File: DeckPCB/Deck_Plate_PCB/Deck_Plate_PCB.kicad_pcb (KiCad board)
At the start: 2 copper layers, 124.1 x 104 mm, 76 parts, among them J1 Raspberry_Pi_2_3, J2 NASA_Telemetry_Interface, J3 NASA PWR_Interface, J8 Board_to_Board, J9 Power, P1 Digital, P10 CONN_01X01, P11 CONN_01X01, P12 CONN_01X01, P13 CONN_01X01, P2 Power, P3 Analog, P4 Analog, P5 PWM, P6 PWM, P7 Communication, P8 CONN_01X01, P9 CONN_01X01, Q2 2N7000, Q3 2N7000, U1 LF356, U10 MAX1044, U11 LF356, U12 LF356, U2 LM2576T-5, U3 D24V25F9, U4 LF356, U5 LM2576T-5, U6 SF_Logic_Level_Conv, U7 Lidar_RangeFinder, U8 ADXL377, U9 TTL_Camera

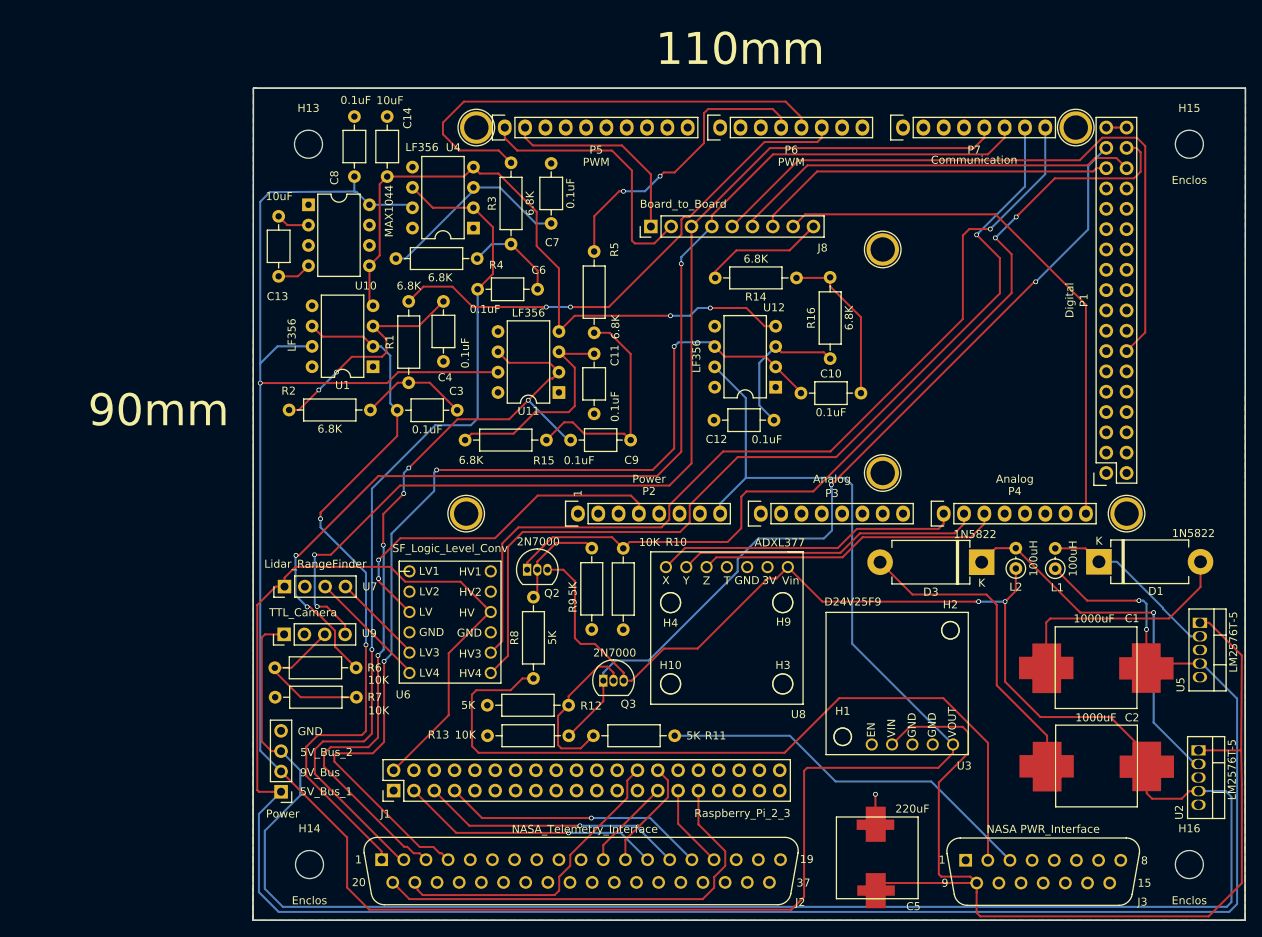
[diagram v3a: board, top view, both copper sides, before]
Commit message: Updated main board to incorporate all 16-bits of telemetry lines
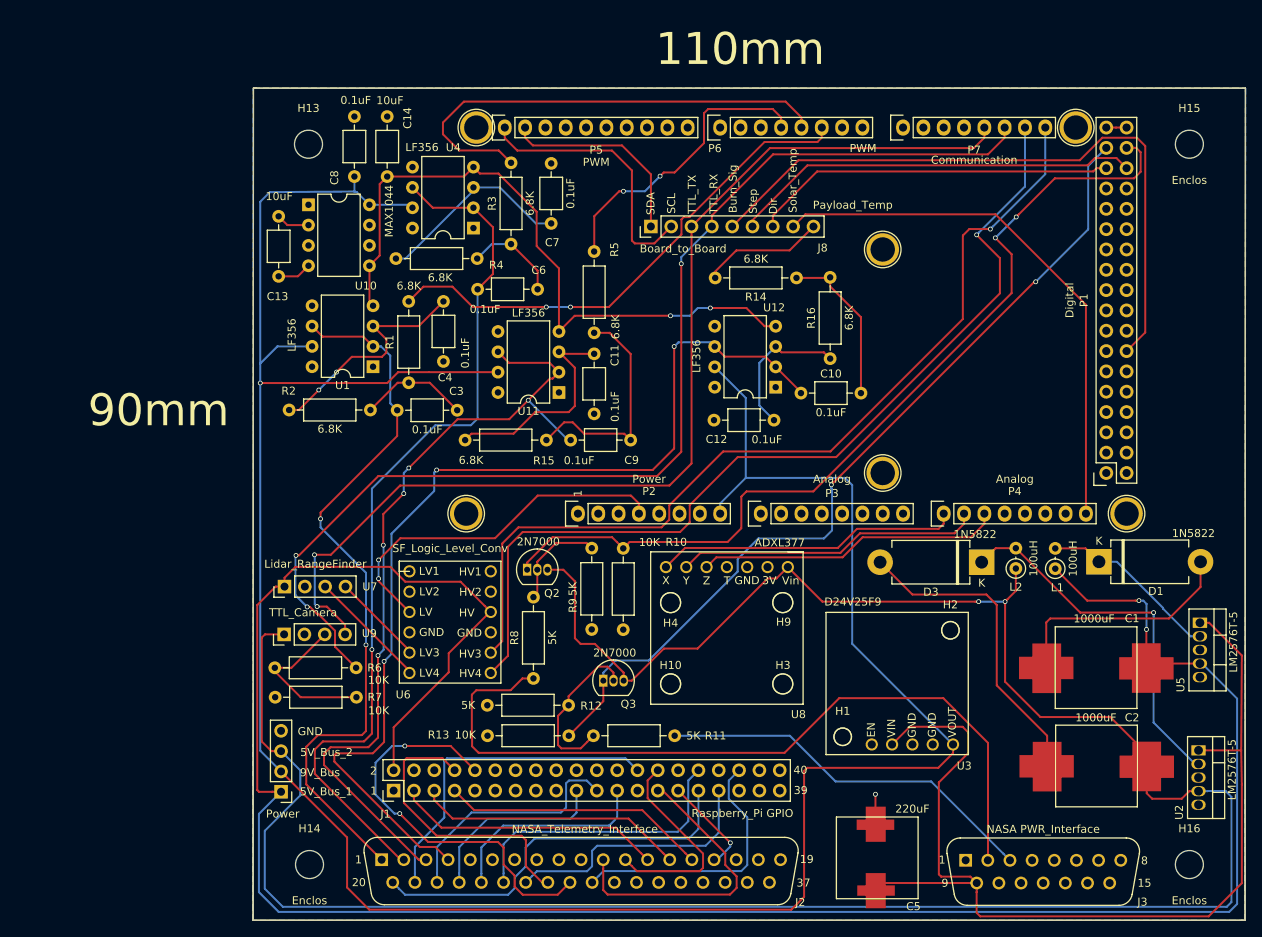
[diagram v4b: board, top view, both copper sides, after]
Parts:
- J1: value Raspberry_Pi_2_3 -> Raspberry_Pi GPIO
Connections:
- net Net-(J1-Pad11) renamed /Bit_16
- J1 pad 10: Net-(J1-Pad10) -> /Bit_14
- J1 pad 19: Net-(J1-Pad19) -> /Bit_9
- J1 pad 21: Net-(J1-Pad21) -> /Bit_8
- J1 pad 23: Net-(J1-Pad23) -> /Bit_10
- J1 pad 32: Net-(J1-Pad32) -> /Bit_11
- J1 pad 33: Net-(J1-Pad33) -> /Bit_12
- J1 pad 36: Net-(J1-Pad36) -> /Bit_15
- J1 pad 8: Net-(J1-Pad8) -> /Bit_13
- J2 pad 22: Net-(J2-Pad22) -> /Bit_8
- J2 pad 23: Net-(J2-Pad23) -> /Bit_9
- J2 pad 24: Net-(J2-Pad24) -> /Bit_10
- J2 pad 25: Net-(J2-Pad25) -> /Bit_11
- J2 pad 26: Net-(J2-Pad26) -> /Bit_12
- J2 pad 27: Net-(J2-Pad27) -> /Bit_13
- J2 pad 28: Net-(J2-Pad28) -> /Bit_14
- J2 pad 29: Net-(J2-Pad29) -> /Bit_15
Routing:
- net /Bit_14: track 0.00 -> 50.7 mm, vias 0 -> 2
- net /Bit_13: track 0.00 -> 36.4 mm
- net /Bit_11: track 0.00 -> 36.0 mm
- net /Bit_15: track 0.00 -> 33.6 mm
- net /Bit_12: track 0.00 -> 33.1 mm
- net /Bit_8: track 0.00 -> 30.1 mm
- net /Bit_10: track 0.00 -> 26.3 mm
- net /Bit_0: track 11.5 -> 37.7 mm
- net /Bit_9: track 0.00 -> 23.6 mm
- net /Bit_1: track 13.9 -> 26.1 mm
- net /Bit_6: track 55.7 -> 49.2 mm
- net /Bit_7: track 37.9 -> 41.6 mm
- net /Bit_5: track 10.5 -> 12.4 mm, vias 0 -> 1
- net /Bit_3: track 33.0 -> 33.7 mm, vias 1 -> 0
- net /Bit_2: track 32.8 -> 33.5 mm, vias 1 -> 0
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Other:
- board text added: "2"
- board text added: "39"
- board text added: "40"
- board text added: "Burn_Sig"
- board text added: "Dir"
- board text added: "Payload_Temp"
- board text added: "SCL"
- board text added: "SDA"
- board text added: "Solar_Temp"
- board text added: "Step"
- board text added: "TTL_RX"
- board text added: "TTL_TX"

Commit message: Updated PCB for NASA analog lines and signal conditioning circuitry. Added Gerber file ZIP for DECK_PLATE_MAIN
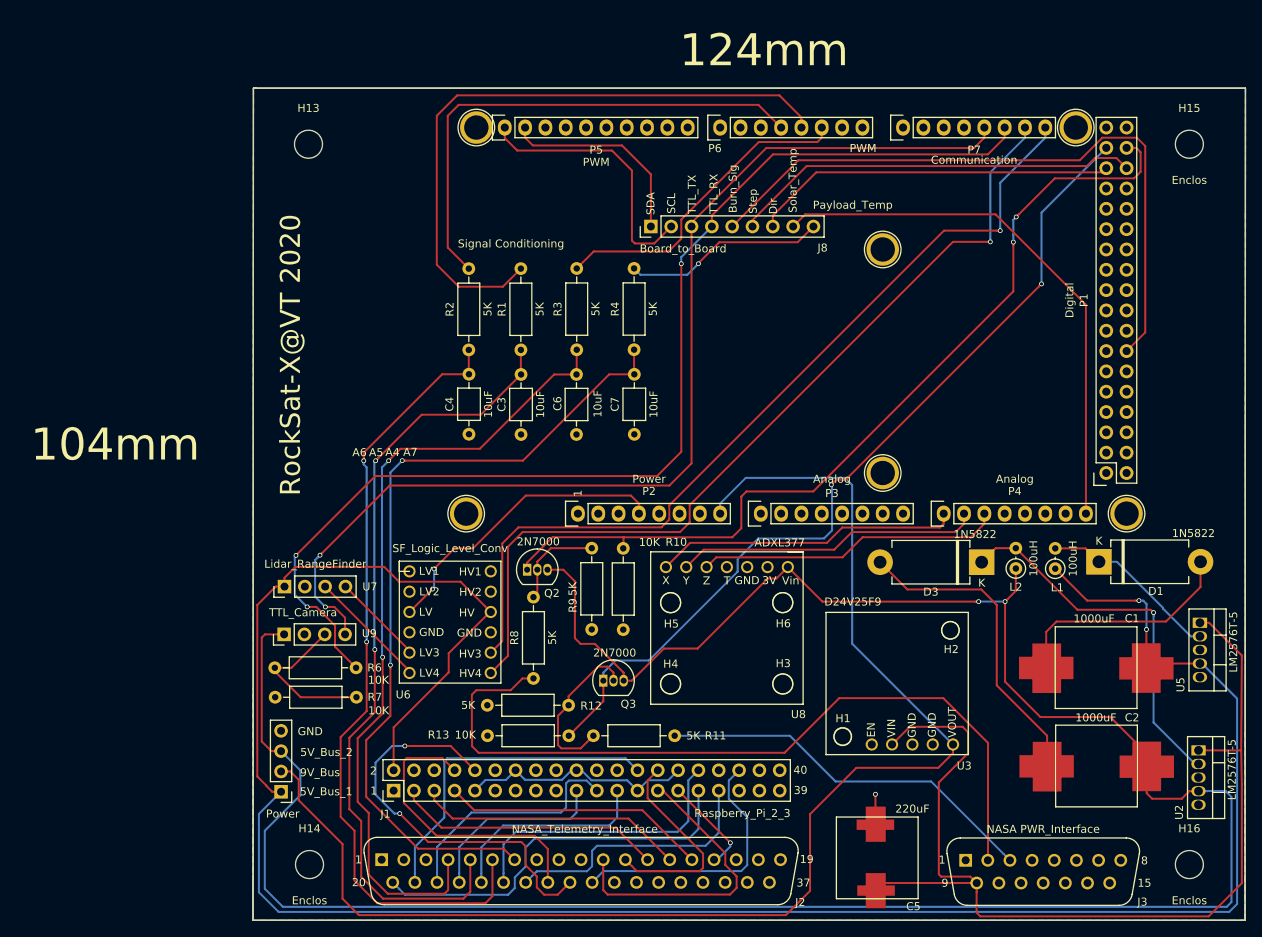
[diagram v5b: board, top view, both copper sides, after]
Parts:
- removed C10, C11, C12, C8, C9: 0.1uF, Capacitor_THT:C_Axial_L3.8mm_D2.6mm_P7.50mm_Horizontal
- removed C13, C14: 10uF, Capacitor_THT:C_Axial_L3.8mm_D2.6mm_P7.50mm_Horizontal
- removed H10, H9: Accel_mount, MountingHole:MountingHole_2.5mm
- removed R14, R15, R16, R5: 6.8K, Resistor_THT:R_Axial_DIN0207_L6.3mm_D2.5mm_P10.16mm_Horizontal
- removed U1, U11, U12, U4: LF356, Package_DIP:DIP-8_W7.62mm
- removed U10: MAX1044, Package_DIP:DIP-8_W7.62mm
- added H5: Accel_mount, Deck_Plate_PCB:Accel_MountingHole_2.5mm, F.Cu at (131.1, 108.3)
- added H6: Accel_mount, Deck_Plate_PCB:Accel_MountingHole_2.5mm, F.Cu at (145.1, 108.3)
- C3, C4, C6, C7: value 0.1uF -> 10uF
- H1, H2: footprint MountingHole:MountingHole_2.2mm_M2 -> Deck_Plate_PCB:9V_MountingHole_2.2mm
- H3, H4: footprint MountingHole:MountingHole_2.5mm -> Deck_Plate_PCB:Accel_MountingHole_2.5mm
- J1: value Raspberry_Pi GPIO -> Raspberry_Pi_2_3
- R1, R2, R3, R4: value 6.8K -> 5K
- moved R4 31.9 mm to (126.5, 76.7), turned to 90 degrees
- moved C7 28.3 mm to (126.6, 87.2)
- moved R2 23.7 mm to (105.9, 76.7), turned to 90 degrees
- moved C6 22.0 mm to (119.3, 87.3), turned to 90 degrees
- moved C4 16.9 mm to (105.9, 87.2), turned to 90 degrees
- moved C3 15.8 mm to (112.4, 87.3), turned to 90 degrees
- moved R3 15.6 mm to (119.4, 76.7)
- moved R1 14.6 mm to (112.4, 76.7)
- moved H4 10.2 mm to (131.1, 118.4)
- moved H3 5.96 mm to (141.1, 114.0)
- moved H2 0.06 mm to (166.1, 111.8)
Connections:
- C3 pad 1: /NASA_Analog_1_OUT -> GND
- C3 pad 2: Net-(C3-Pad2) -> /NASA_Analog_5_OUT
- C4 pad 1: Net-(C4-Pad1) -> GND
- C4 pad 2: GND -> /NASA_Analog_6_OUT
- C6 pad 1: /NASA_Analog_2_OUT -> GND
- C6 pad 2: Net-(C6-Pad2) -> /NASA_Analog_4_OUT
- C7 pad 1: Net-(C7-Pad1) -> GND
- C7 pad 2: GND -> /NASA_Analog_7_OUT
- J2 pad 1: /NASA_Analog_1_OUT -> Net-(J2-Pad1)
- J2 pad 2: /NASA_Analog_2_OUT -> Net-(J2-Pad2)
- J2 pad 3: /NASA_Analog_3_OUT -> Net-(J2-Pad3)
- J2 pad 5: Net-(J2-Pad5) -> /NASA_Analog_5_OUT
- J2 pad 6: Net-(J2-Pad6) -> /NASA_Analog_6_OUT
- J2 pad 7: Net-(J2-Pad7) -> /NASA_Analog_7_OUT
- P1 pad 36: Net-(P1-Pad35) -> Net-(P1-Pad36)
- P6 pad 4: /NASA_Analog_3_IN -> /NASA_Analog_6_IN
- P6 pad 5: /NASA_Analog_2_IN -> /NASA_Analog_5_IN
- P6 pad 6: /NASA_Analog_1_IN -> /NASA_Analog_4_IN
- R1 pad 1: Net-(C3-Pad2) -> /NASA_Analog_5_OUT
- R1 pad 2: /NASA_Analog_1_IN -> /NASA_Analog_5_IN
- R2 pad 1: Net-(C4-Pad1) -> /NASA_Analog_6_OUT
- R2 pad 2: Net-(C3-Pad2) -> /NASA_Analog_6_IN
- R3 pad 1: Net-(C6-Pad2) -> /NASA_Analog_4_OUT
- R3 pad 2: /NASA_Analog_2_IN -> /NASA_Analog_4_IN
- R4 pad 1: Net-(C7-Pad1) -> /NASA_Analog_7_OUT
- R4 pad 2: Net-(C6-Pad2) -> /PayloadTemp
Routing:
- net /9V_Bus: track 318.0 -> 169.2 mm, vias 1 -> 0
- net /NASA_Analog_2_OUT: track 110.9 -> 0.00 mm, vias 1 -> 0
- net /NASA_Analog_7_OUT: track 0.00 -> 102.3 mm, vias 0 -> 2
- net /NASA_Analog_3_OUT: track 101.7 -> 0.00 mm, vias 5 -> 0
- net /NASA_Analog_6_OUT: track 0.00 -> 99.3 mm, vias 0 -> 2
- net /NASA_Analog_5_OUT: track 0.00 -> 98.9 mm, vias 0 -> 2
- net /NASA_Analog_1_OUT: track 91.2 -> 0.00 mm, vias 2 -> 0
- net /-9V_Bus: track 84.1 -> 0.00 mm, vias 2 -> 0
- net /NASA_Analog_5_IN: track 0.00 -> 80.3 mm
- net /NASA_Analog_1_IN: track 64.6 -> 0.00 mm, vias 2 -> 0
- net /NASA_Analog_6_IN: track 0.00 -> 63.6 mm
- net /NASA_Analog_2_IN: track 59.4 -> 0.00 mm
- net /NASA_Analog_4_IN: track 0.00 -> 40.1 mm
- net /NASA_Analog_3_IN: track 37.2 -> 0.00 mm, vias 2 -> 0
- net GND: track 3.89 -> 33.4 mm
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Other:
- board text added: "104mm"
- board text added: "124mm"
- board text added: "A4"
- board text added: "A5"
- board text added: "A6"
- board text added: "A7"
- board text added: "RockSat-X@VT 2020"
- board text added: "Signal Conditioning"
- board text removed: "110mm"
- board text removed: "90mm"

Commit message: Updated Main_Deck_Plate and Daughter_Board to fit Electronics Enclosure internal dimensions. Created all PCB Gerber files. Created all PCB PNG images. Created all PCB STEP files for mechanical integration. Implemented all design review comments and corrections.
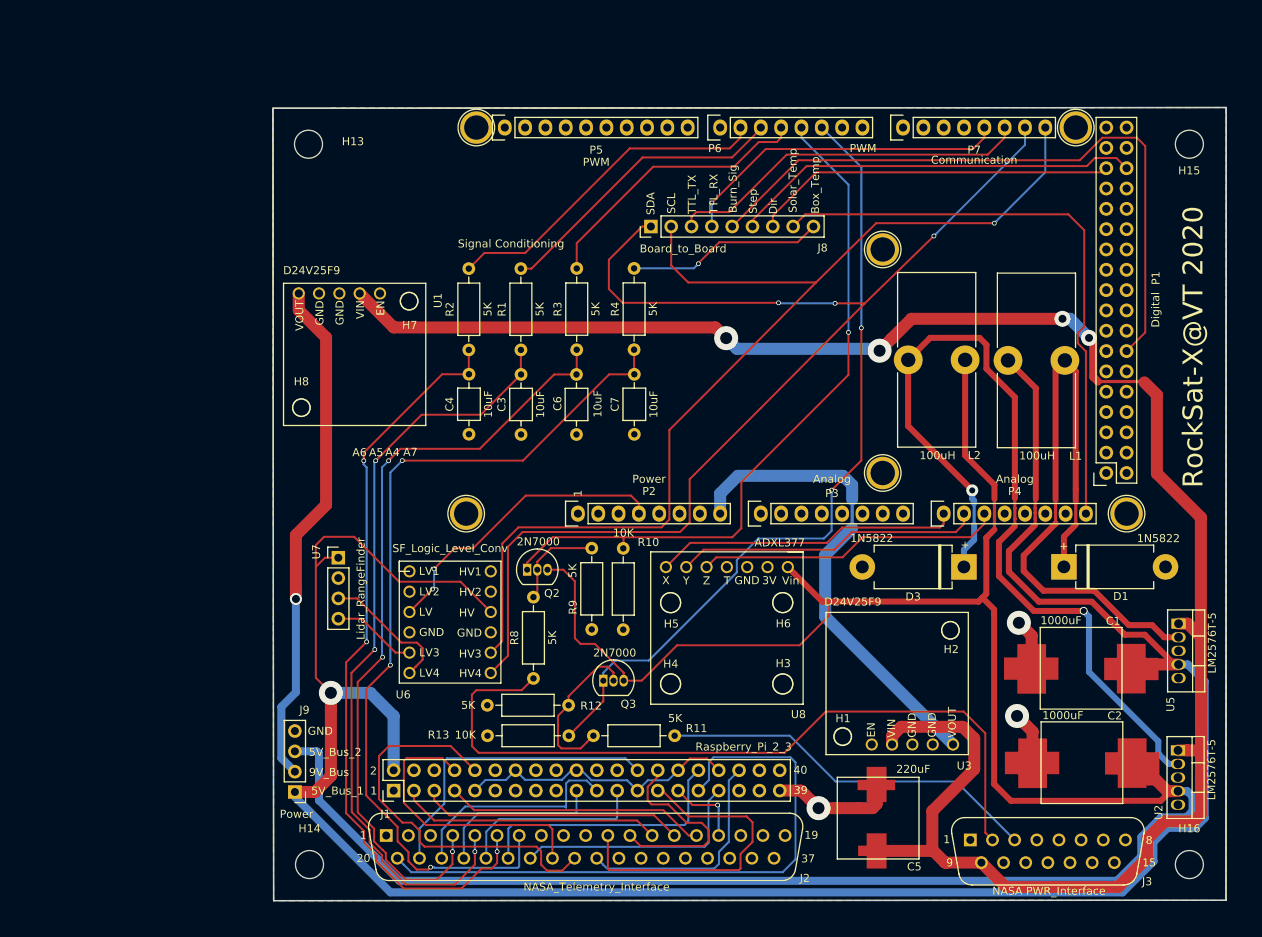
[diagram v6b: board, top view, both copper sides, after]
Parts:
- removed R6, R7: 10K, Resistor_THT:R_Axial_DIN0207_L6.3mm_D2.5mm_P10.16mm_Horizontal
- removed U9: TTL_Camera, Connector_PinHeader_2.54mm:PinHeader_1x04_P2.54mm_Vertical
- added H7: 9V_mount, Deck_Plate_PCB:9V_MountingHole_2.2mm, F.Cu at (98.4, 70.7)
- added H8: 9V_mount, Deck_Plate_PCB:9V_MountingHole_2.2mm, F.Cu at (85.0, 84.0)
- added U1: D24V25F9, Deck_Plate_PCB:D24V25F9, F.Cu at (84.0, 69.6)
- L1, L2: footprint Inductor_THT:L_Axial_L5.3mm_D2.2mm_P2.54mm_Vertical_Vishay_IM-1 -> Inductor_THT:L_Toroid_Vertical_L21.6mm_W9.5mm_P7.11mm_Pulse_C
- moved L2 26.8 mm to (167.9, 77.9), turned to 270 degrees
- moved L1 26.7 mm to (173.3, 78.0)
- moved U7 7.63 mm to (89.6, 102.7), turned to 0 degrees
- moved C5 4.97 mm to (155.6, 141.5)
- moved D1 4.42 mm to (180.3, 103.8)
- moved J2 3.08 mm to (95.6, 137.4)
- moved U5 2.67 mm to (194.6, 110.9)
- moved J3 2.61 mm to (168.6, 137.9)
- moved U2 2.56 mm to (194.5, 126.7)
- moved D3 2.30 mm to (167.8, 103.8)
- moved C1 1.88 mm to (193.3, 124.2)
- moved C2 1.87 mm to (193.4, 136.0)
- moved J9 1.73 mm to (84.2, 131.9)
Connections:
- net /PayloadTemp renamed /Box_Temp
- C1 pad 2: Net-(C1-Pad2) -> GND
- C2 pad 2: Net-(C2-Pad2) -> GND
- D1 pad 2: Net-(C1-Pad2) -> GND
- D3 pad 2: Net-(C2-Pad2) -> GND
- J8 pad 1: /SDA -> /20(SDA)
- J8 pad 2: /SCL -> /21(SCL)
- J9 pad 2: /9V_Bus -> /9V_Bus_2
- P1 pad 33: /TE_B -> Net-(P1-Pad33)
- P1 pad 34: /TE_A -> Net-(P1-Pad34)
- P2 pad 8: /9V_Bus -> /9V_Bus_1
- P6 pad 2: /6(**) -> /NASA_Analog_6_IN
- P6 pad 3: /5(**) -> /NASA_Analog_5_IN
- P6 pad 4: /NASA_Analog_6_IN -> /NASA_Analog_4_IN
- P6 pad 5: /NASA_Analog_5_IN -> /TE_A
- P6 pad 6: /NASA_Analog_4_IN -> /TE_B
- P7 pad 5: /TTL_TX -> /TTL_RX
- P7 pad 6: /TTL_RX -> /TTL_TX
- U3 pad 5: /9V_Bus -> /9V_Bus_1
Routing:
- net /9V_Bus: track 169.2 -> 0.00 mm
- net /28V_GSE_2: track 128.2 -> 247.0 mm, vias 0 -> 4
- net /TTL_RX: track 144.5 -> 41.7 mm, vias 3 -> 1
- net /TTL_TX: track 135.9 -> 45.7 mm, vias 2 -> 0
- net /9V_Bus_2: track 0.00 -> 64.2 mm, vias 0 -> 1
- net Net-(D3-Pad1): track 47.0 -> 109.8 mm, vias 1 -> 2
- net /9V_Bus_1: track 0.00 -> 60.9 mm
- net Net-(D1-Pad1): track 22.7 -> 79.5 mm
- net /NASA_Analog_5_IN: track 80.3 -> 37.4 mm
- net /20(SDA): track 110.1 -> 150.8 mm, vias 1 -> 3
- net Net-(C2-Pad2): track 39.6 -> 0.00 mm
- net /SCL: track 33.6 -> 0.00 mm
- net GND: track 33.4 -> 64.7 mm, vias 1 -> 3
- net /Bit_6: track 49.2 -> 79.1 mm
- net Net-(C1-Pad2): track 29.3 -> 0.00 mm
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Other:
- board size 124.1 x 104 mm -> 119.2 x 99.1 mm
- board text added: "+"
- board text added: "119mm"
- board text added: "99mm"
- board text added: "Box_Temp"
- board text added: "Farid Bazzal Chris Mattson Eric Williams Hunain Shamsi"
- board text added: "Jacob Di Girolamo Kathryn Robertson Matt Brockmeyer Riya Sareen Spencer Buebel Surabhi Srivastava"
- board text added: "Kristofer Stone Nicholas Jones Brennan Rausch Danny Flynn"
- board text added: "RockSat-X@VT 2020 Team"
- board text removed: "104mm"
- board text removed: "124mm"
- board text removed: "Payload_Temp"
